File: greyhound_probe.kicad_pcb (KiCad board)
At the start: 4 copper layers, 40.6 x 23 mm, 44 parts, among them J1 USB_C_Receptacle_USB2.0, J2 Conn_01x04_Male, J3 FTSH-105-01-L-DV-K-TR, Q1 IRLML6401, SW1 SW_SPDT, U1 XC6206P332MR, U2 USBLC6-2SC6, U3 STM32F072CBUx

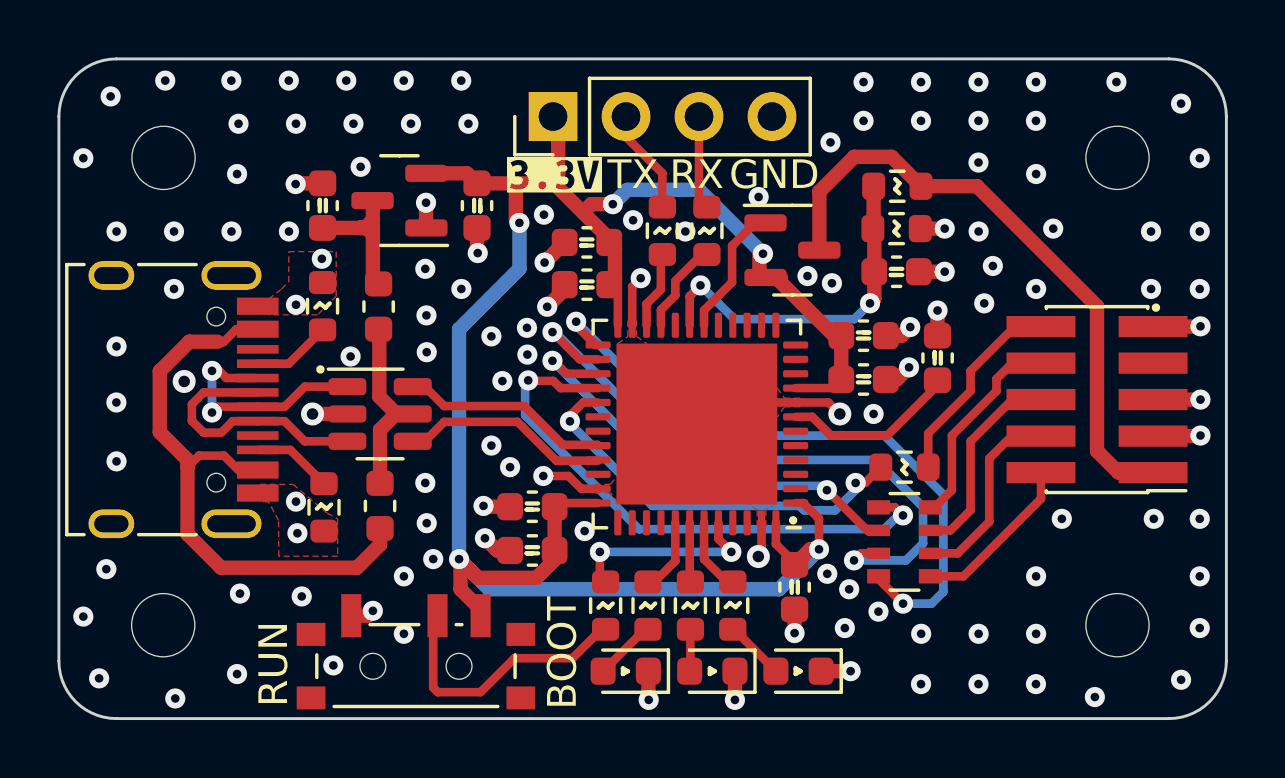
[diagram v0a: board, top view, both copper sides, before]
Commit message: Better spacing of a few signal traces and vias
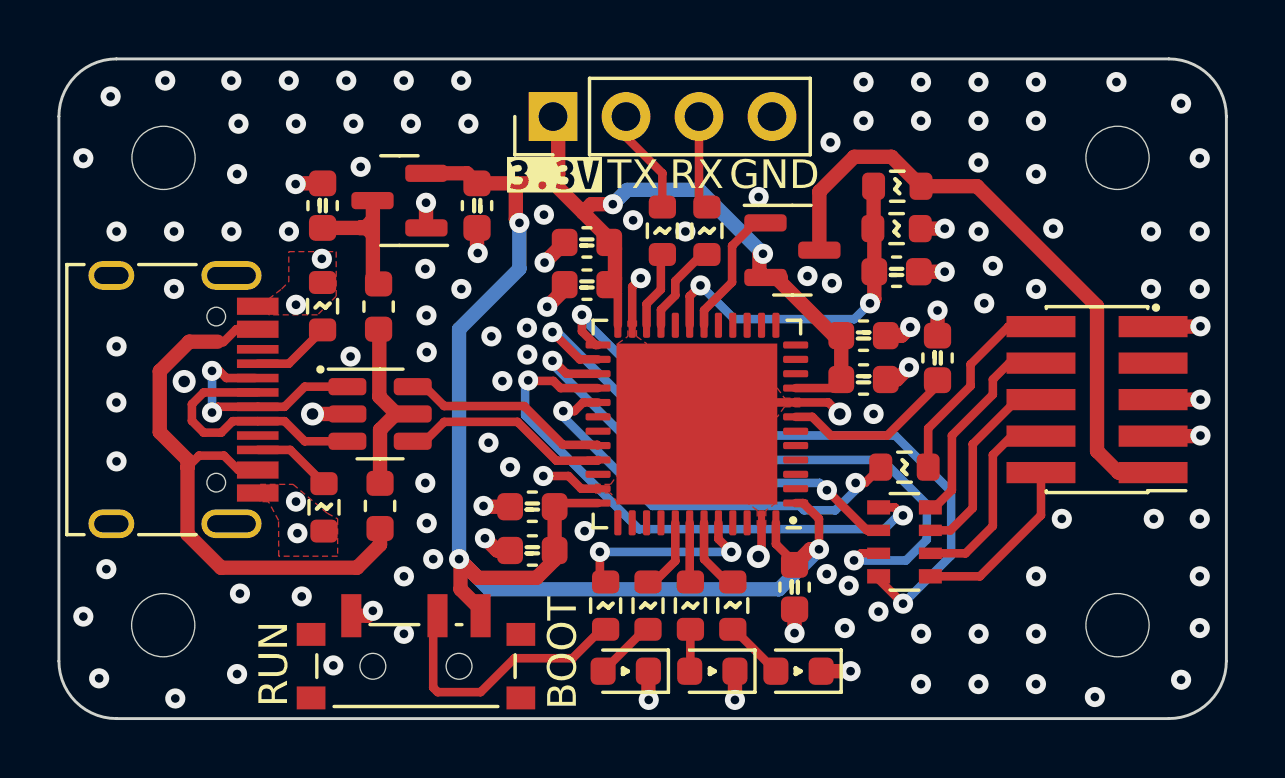
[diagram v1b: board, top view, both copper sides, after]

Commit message: Added SWD, rearranged bottom part
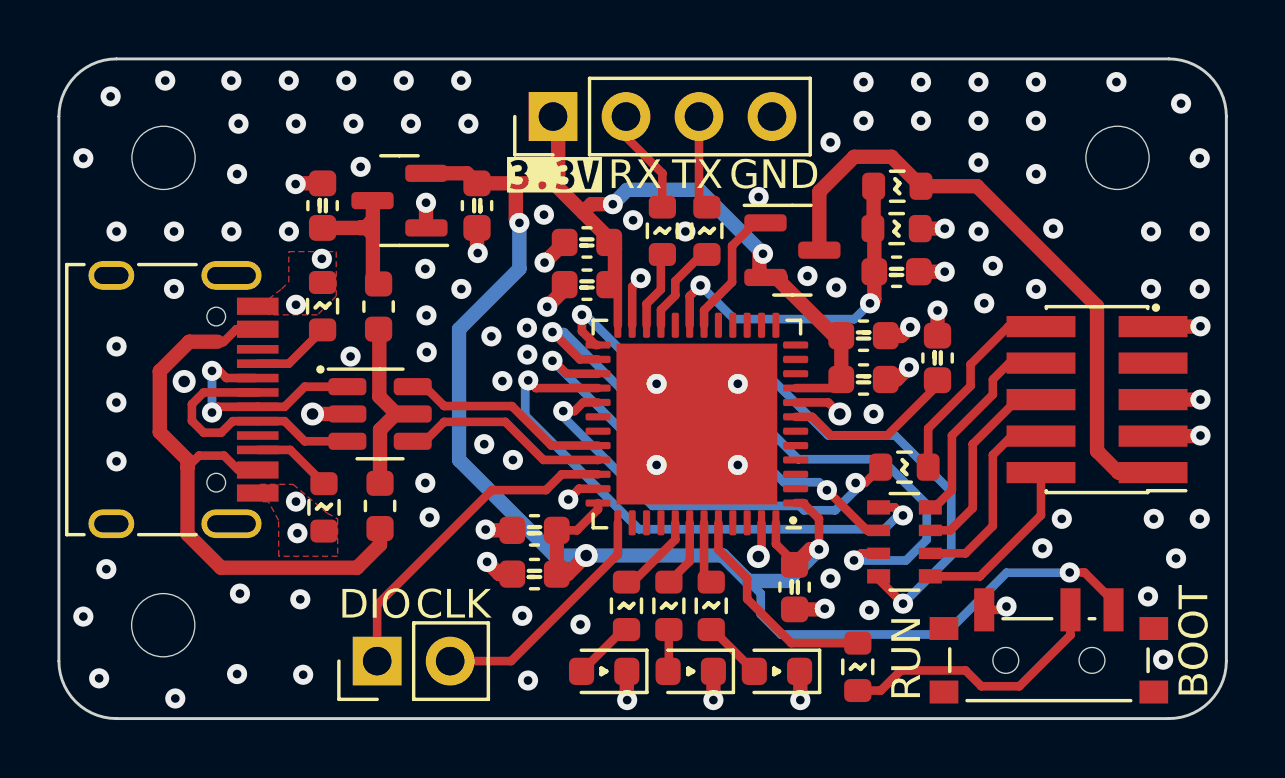
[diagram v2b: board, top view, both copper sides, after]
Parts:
- removed H2: MountingHole, MountingHole:MountingHole_2.2mm_M2
- removed kibuzzard-6313B2B7: G***, kibuzzard-6313B2B7
- added J4: Conn_01x02_Male, Connector_PinHeader_2.54mm:PinHeader_1x02_P2.54mm_Vertical, F.Cu at (130.1, 87.2)
- added kibuzzard-6360FEA6: G***, kibuzzard-6360FEA6, B.Cu at (157.6, 77.8)
- moved SW1 22.0 mm to (153.4, 86.8)
- moved R10 9.03 mm to (146.8, 87.3)
- moved C9 0.83 mm to (135.6, 84.1)
- moved C10 0.83 mm to (135.6, 82.6)
- moved D2 0.75 mm to (141.0, 87.5)
- moved D3 0.75 mm to (144.0, 87.5)
- moved D1 0.75 mm to (138.0, 87.5)
- moved R5 0.75 mm to (138.8, 85.2)
- moved R6 0.75 mm to (140.2, 85.2)
- moved R7 0.75 mm to (141.7, 85.2)
- renumbered R8 to R10, R9 to R8, R10 to R9
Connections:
- U3 pad 34: unconnected-(U3-Pad34) -> /SWDIO
- U3 pad 37: unconnected-(U3-Pad37) -> /SWCLK
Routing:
- net /SWDIO: track 0.00 -> 11.5 mm
- net +3.3V: track 71.3 -> 79.9 mm, vias 5 -> 6
- net /SWCLK: track 0.00 -> 8.48 mm
- net GND: track 32.7 -> 28.2 mm, vias 126 -> 120
- net /BOOT: track 6.90 -> 7.55 mm, vias 2 -> 0
- net Net-(R7-Pad1): track 2.77 -> 2.17 mm
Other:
- board text added: "CLK"
- board text added: "DIO"

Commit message: Added in series resistor to mosfet gate, nrst pullup, more regulator caps, reduced via sharing
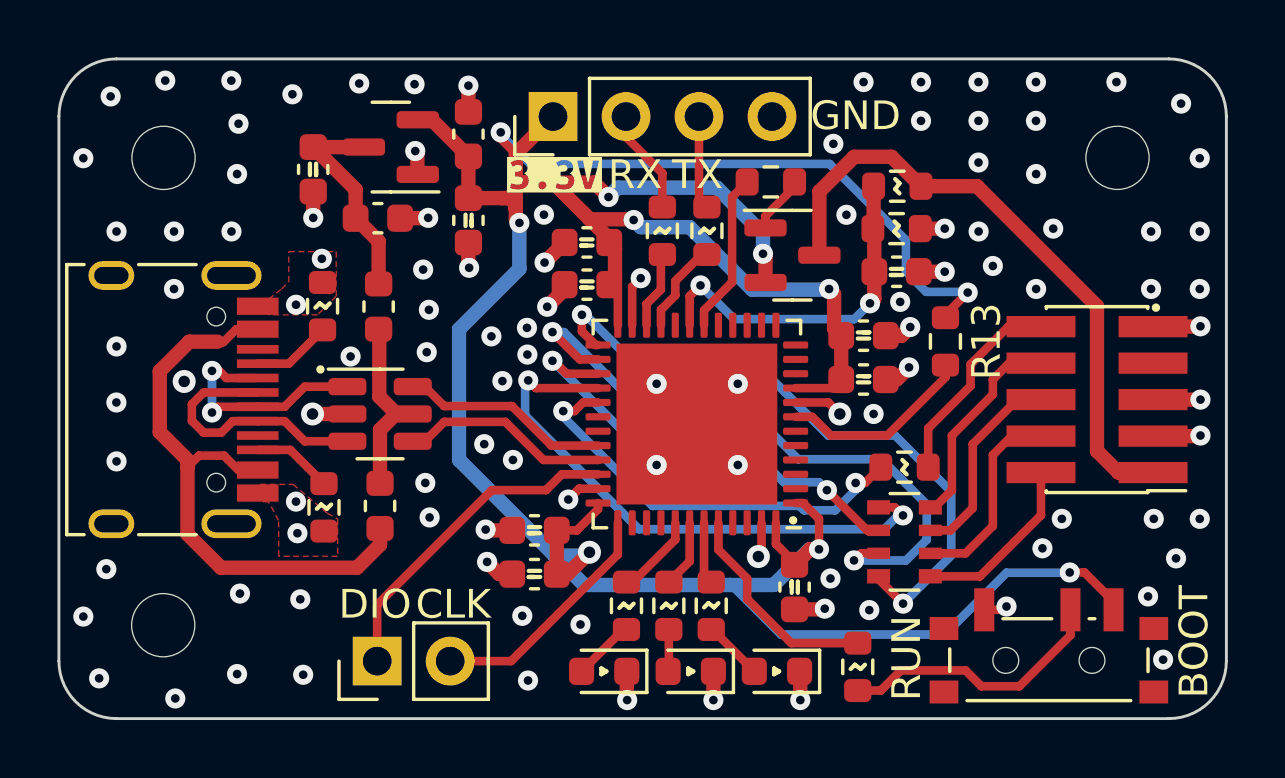
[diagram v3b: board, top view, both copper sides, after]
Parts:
- removed the C11 at (149.6, 76.6)
- added C1: 4.7uF, Capacitor_SMD:C_0603_1608Metric, F.Cu at (130.1, 71.7)
- added C3: 4.7uF, Capacitor_SMD:C_0603_1608Metric, F.Cu at (133.2, 68.8)
- added R13: 10k, Resistor_SMD:R_0603_1608Metric, F.Cu at (149.8, 76.0)
- added R5: 1k, Resistor_SMD:R_0603_1608Metric, F.Cu at (143.8, 70.5)
- moved U1 1.89 mm to (130.6, 69.3)
- moved C2 1.30 mm to (127.8, 70.0), turned to -90 degrees
- moved C4 0.59 mm to (133.2, 71.8)
- moved Q1 0.18 mm to (144.5, 73.0)
- renumbered C8 to C10, C9 to C11, C10 to C12, C1 to C2, C2 to C4, C3 to C5, C4 to C6, C5 to C7, C6 to C8, C7 to C9, H3 to H1, H4 to H2, H1 to H3, R9 to R10, R10 to R11, R11 to R12, R5 to R6, R6 to R7, R7 to R8, R8 to R9
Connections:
- Q1 pad 1: /TARGET_POWER -> Net-(Q1-Pad1)
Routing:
- net +3.3V: track 79.9 -> 116.2 mm, vias 6 -> 10
- net Net-(Q1-Pad1): track 0.00 -> 2.02 mm
- net VBUS: track 7.00 -> 5.85 mm
- net Net-(C1-Pad1): track 6.44 -> 7.47 mm
- net /TARGET_POWER: track 4.66 -> 5.61 mm
- net GND: track 28.2 -> 29.2 mm, vias 120 -> 108
- net /NRST: track 6.11 -> 6.75 mm
